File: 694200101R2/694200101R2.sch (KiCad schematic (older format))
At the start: 264 parts, among them J1 USB_C_Receptacle_USB2.0, J2 Conn_01x06_Male, J3 Conn_01x02_Male, SW1 MX_SW, SW10 MX_SW, SW100 MX_SW, SW101 MX_SW, SW102 MX_SW, SW103 MX_SW, SW104 MX_SW, SW105 MX_SW, SW106 MX_SW, SW107 MX_SW, SW108 SW_SPST, SW109 SW_SPDT, SW11 MX_SW, SW12 MX_SW, SW13 MX_SW, SW14 MX_SW, SW15 MX_SW, SW16 MX_SW, SW17 MX_SW, SW18 MX_SW, SW19 MX_SW, SW2 MX_SW, SW20 MX_SW, SW21 MX_SW, SW22 MX_SW, SW23 MX_SW, SW24 MX_SW, SW25 MX_SW, SW26 MX_SW, SW27 MX_SW, SW28 MX_SW, SW29 MX_SW, SW3 MX_SW, SW30 MX_SW, SW31 MX_SW, SW32 MX_SW, SW33 MX_SW, SW34 MX_SW, SW35 MX_SW, SW36 MX_SW, SW37 MX_SW, SW38 MX_SW, SW39 MX_SW, SW4 MX_SW, SW40 MX_SW, SW41 MX_SW, SW42 MX_SW, SW43 MX_SW, SW44 MX_SW, SW45 MX_SW, SW46 MX_SW, SW47 MX_SW, SW48 MX_SW, SW49 MX_SW, SW5 MX_SW, SW50 MX_SW, SW51 MX_SW, SW52 MX_SW, SW53 MX_SW, SW54 MX_SW, SW55 MX_SW, SW56 MX_SW, SW57 MX_SW, SW58 MX_SW, SW59 MX_SW, SW6 MX_SW, SW60 MX_SW, SW61 MX_SW, SW62 MX_SW, SW63 MX_SW, SW64 MX_SW, SW65 MX_SW, SW66 MX_SW, SW67 MX_SW, SW68 MX_SW, SW69 MX_SW, SW7 MX_SW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

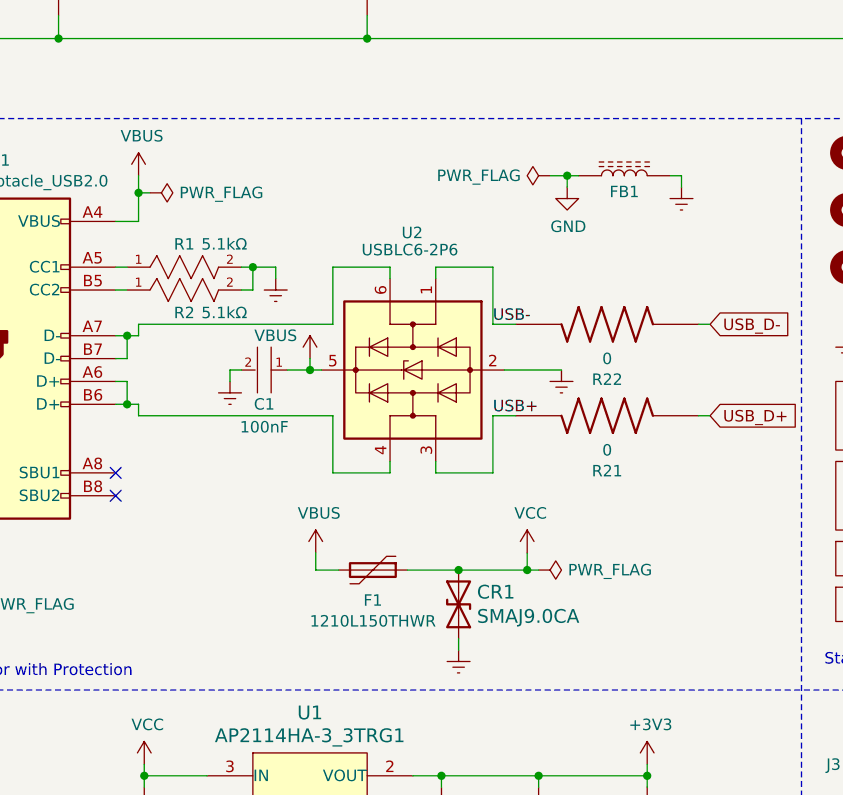
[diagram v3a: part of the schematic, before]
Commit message: Fix Ferrite Bead Placement
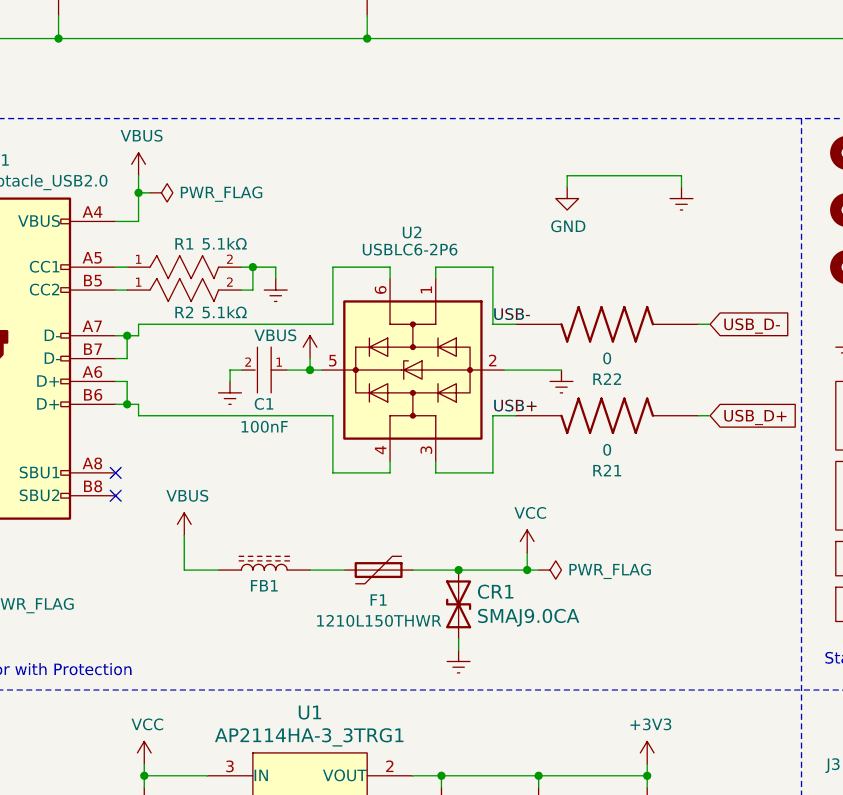
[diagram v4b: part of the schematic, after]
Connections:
- net Earth: now also C10.2, C2.2, C25.2, C3.2, C4.2, C5.2, C6.2, C7.2, C9.2, ENC1.3, ENC1.C (COM), J2.2 (Pin_2), R23.2, SW108.2 (B), U1.1 (GND), U1.4 (GND), U3.12 (VSSA), U3.18 (VSS), U3.31 (VSS), U3.47 (VSS), U3.63 (VSS), U4.1 (A0), U4.3 (A2), U4.4 (GND), U4.7 (WP), Y1.2 (GND), Y1.4 (GND); no longer FB1.1
- net VBUS: now also FB1.2; no longer F1.2
- removed net GND: C10.2, C2.2, C25.2, C3.2, C4.2, C5.2, C6.2, C7.2, C9.2, ENC1.3, ENC1.C (COM), FB1.2, J2.2 (Pin_2), R23.2, SW108.2 (B), U1.1 (GND), U1.4 (GND), U3.12 (VSSA), U3.18 (VSS), U3.31 (VSS), U3.47 (VSS), U3.63 (VSS), U4.1 (A0), U4.3 (A2), U4.4 (GND), U4.7 (WP), Y1.2 (GND), Y1.4 (GND)
- new net: F1.2, FB1.1
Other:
- moved on the sheet: F1, FB1
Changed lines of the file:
@@
 	3550 6875 3550 6800
 Wire Wire Line
-	2625 6800 2625 6875
+	2050 6725 2050 6875
 $Comp
 L power:PWR_FLAG #FLG0102
@@
 L Device:Polyfuse F1
 U 1 1 65E04245
-P 2875 6875
-F 0 "F1" V 3008 6875 50  0000 C CNN
-F 1 "1210L150THWR" V 3099 6875 50  0000 C CNN
-F 2 "Fuse:Fuse_1210_3225Metric_Castellated" H 2925 6675 50  0001 L CNN
-F 3 "~" H 2875 6875 50  0001 C CNN
-	1    2875 6875
+P 2900 6875
+F 0 "F1" V 3033 6875 50  0000 C CNN
+F 1 "1210L150THWR" V 3124 6875 50  0000 C CNN
+F 2 "Fuse:Fuse_1210_3225Metric_Castellated" H 2950 6675 50  0001 L CNN
+F 3 "~" H 2900 6875 50  0001 C CNN
+	1    2900 6875
 	0    1    1    0
 $EndComp
@@
 NoConn ~ 10775 7975
 $Comp
-L power:PWR_FLAG #FLG0104
-U 1 1 6796B8B4
-P 3650 5150
-F 0 "#FLG0104" H 3650 5225 50  0001 C CNN
-F 1 "PWR_FLAG" V 3650 5277 50  0000 L CNN
-F 2 "" H 3650 5150 50  0001 C CNN
-F 3 "~" H 3650 5150 50  0001 C CNN
-	1    3650 5150
-	0    -1   -1   0
-$EndComp
-Wire Wire Line
-	3650 5150 3725 5150
-Connection ~ 3725 5150
-$Comp
 L Power_Protection:USBLC6-2P6 U2
 U 1 1 67AF17E5
@@
 L cldg:BBUP00160808600Y00 FB1
 U 1 1 604967EC
-P 3925 5250
-F 0 "FB1" H 3875 5250 50  0000 C BNN
-F 1 "BBUP00160808600Y00" H 3875 5484 50  0001 C CNN
-F 2 "Resistor_SMD:R_0603_1608Metric" H 3925 5250 50  0001 C CNN
-F 3 "" H 3925 5250 50  0001 C CNN
-	1    3925 5250
+P 2350 6975
+F 0 "FB1" H 2300 6975 50  0000 C BNN
+F 1 "BBUP00160808600Y00" H 2300 7209 50  0001 C CNN
+F 2 "Resistor_SMD:R_0603_1608Metric" H 2350 6975 50  0001 C CNN
+F 3 "" H 2350 6975 50  0001 C CNN
+	1    2350 6975
 	-1   0    0    -1
 $EndComp
@@
 L power:VBUS #PWR0112
 U 1 1 629BAD62
-P 2625 6800
-F 0 "#PWR0112" H 2625 6650 50  0001 C CNN
-F 1 "VBUS" H 2640 6973 50  0000 C CNN
-F 2 "" H 2625 6800 50  0001 C CNN
-F 3 "" H 2625 6800 50  0001 C CNN
-	1    2625 6800
-	1    0    0    -1
-$EndComp
-Wire Wire Line
-	3725 5150 3775 5150
-Wire Wire Line
-	4175 5150 4225 5150
-Wire Wire Line
-	3025 6875 3250 6875
-Wire Wire Line
-	2625 6875 2725 6875
+P 2050 6725
+F 0 "#PWR0112" H 2050 6575 50  0001 C CNN
+F 1 "VBUS" H 2065 6898 50  0000 C CNN
+F 2 "" H 2050 6725 50  0001 C CNN
+F 3 "" H 2050 6725 50  0001 C CNN
+	1    2050 6725
+	1    0    0    -1
+$EndComp
+Wire Wire Line
+	3050 6875 3250 6875
 Wire Wire Line
 	3250 6875 3550 6875
@@
 Text Notes 11725 8925 0    50   ~ 0
 EEPROM - User Settings Storage
+Wire Wire Line
+	2600 6875 2750 6875
+Wire Wire Line
+	2050 6875 2200 6875
+Wire Wire Line
+	3725 5150 4225 5150
 $EndSCHEMATC

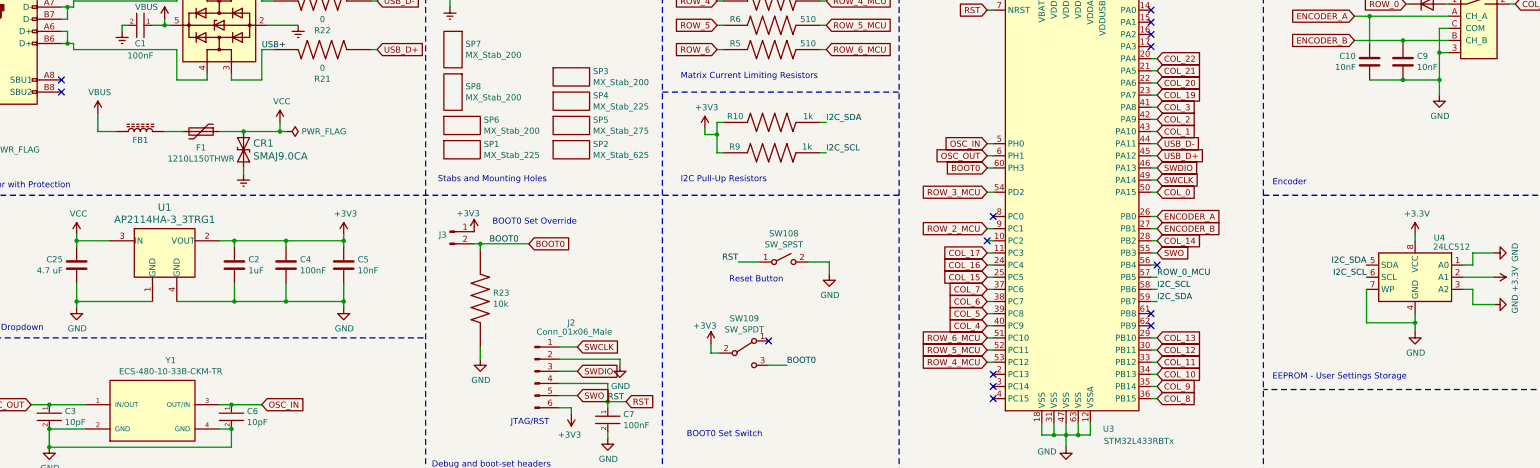
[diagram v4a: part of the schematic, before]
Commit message: Updated Address in schematic
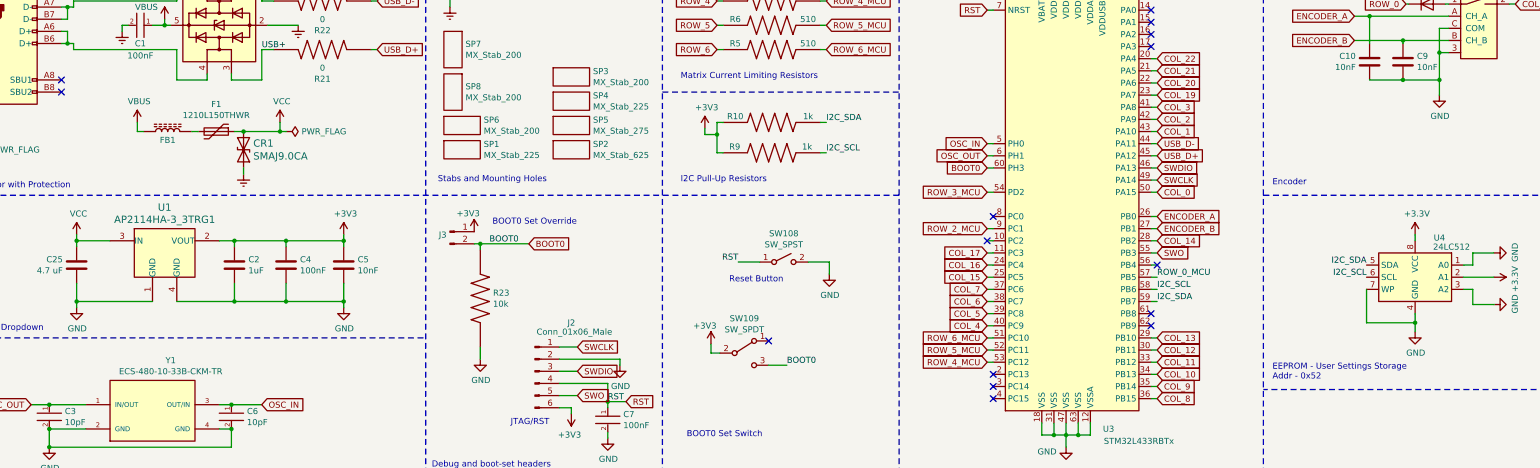
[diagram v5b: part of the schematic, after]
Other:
- note added: "EEPROM - User Settings Storage\nAddr - 0x52"
- note removed: "EEPROM - User Settings Storage"
- moved on the sheet: F1, FB1
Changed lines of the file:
@@
 	3550 6875 3550 6800
 Wire Wire Line
-	2050 6725 2050 6875
+	2375 6800 2375 6875
 $Comp
 L power:PWR_FLAG #FLG0102
@@
 L Device:Polyfuse F1
 U 1 1 65E04245
-P 2900 6875
-F 0 "F1" V 3033 6875 50  0000 C CNN
-F 1 "1210L150THWR" V 3124 6875 50  0000 C CNN
-F 2 "Fuse:Fuse_1210_3225Metric_Castellated" H 2950 6675 50  0001 L CNN
-F 3 "~" H 2900 6875 50  0001 C CNN
-	1    2900 6875
+P 3025 6875
+F 0 "F1" V 2800 6875 50  0000 C CNN
+F 1 "1210L150THWR" V 2891 6875 50  0000 C CNN
+F 2 "Fuse:Fuse_1210_3225Metric_Castellated" H 3075 6675 50  0001 L CNN
+F 3 "~" H 3025 6875 50  0001 C CNN
+	1    3025 6875
 	0    1    1    0
 $EndComp
@@
 L cldg:BBUP00160808600Y00 FB1
 U 1 1 604967EC
-P 2350 6975
-F 0 "FB1" H 2300 6975 50  0000 C BNN
-F 1 "BBUP00160808600Y00" H 2300 7209 50  0001 C CNN
-F 2 "Resistor_SMD:R_0603_1608Metric" H 2350 6975 50  0001 C CNN
-F 3 "" H 2350 6975 50  0001 C CNN
-	1    2350 6975
+P 2575 6975
+F 0 "FB1" H 2525 6975 50  0000 C BNN
+F 1 "BBUP00160808600Y00" H 2525 7209 50  0001 C CNN
+F 2 "Resistor_SMD:R_0603_1608Metric" H 2575 6975 50  0001 C CNN
+F 3 "" H 2575 6975 50  0001 C CNN
+	1    2575 6975
 	-1   0    0    -1
 $EndComp
@@
 L power:VBUS #PWR0112
 U 1 1 629BAD62
-P 2050 6725
-F 0 "#PWR0112" H 2050 6575 50  0001 C CNN
-F 1 "VBUS" H 2065 6898 50  0000 C CNN
-F 2 "" H 2050 6725 50  0001 C CNN
-F 3 "" H 2050 6725 50  0001 C CNN
-	1    2050 6725
-	1    0    0    -1
-$EndComp
-Wire Wire Line
-	3050 6875 3250 6875
+P 2375 6800
+F 0 "#PWR0112" H 2375 6650 50  0001 C CNN
+F 1 "VBUS" H 2390 6973 50  0000 C CNN
+F 2 "" H 2375 6800 50  0001 C CNN
+F 3 "" H 2375 6800 50  0001 C CNN
+	1    2375 6800
+	1    0    0    -1
+$EndComp
+Wire Wire Line
+	3175 6875 3250 6875
 Wire Wire Line
 	3250 6875 3550 6875
@@
 	14375 4900 14375 9000
 Text Notes 11725 8925 0    50   ~ 0
-EEPROM - User Settings Storage
-Wire Wire Line
-	2600 6875 2750 6875
-Wire Wire Line
-	2050 6875 2200 6875
+EEPROM - User Settings Storage\nAddr - 0x52
+Wire Wire Line
+	2825 6875 2875 6875
+Wire Wire Line
+	2375 6875 2425 6875
 Wire Wire Line
 	3725 5150 4225 5150

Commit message: sch review
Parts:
- removed J3: Conn_01x02_Male, Connector_PinHeader_2.54mm:PinHeader_1x02_P2.54mm_Vertical, symbol Connector:Conn_01x02_Male
- C2: value 1uF -> 4.7 uF; footprint Capacitor_SMD:C_0603_1608Metric -> Capacitor_SMD:C_0805_2012Metric
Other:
- note removed: "BOOT0 Set Override"
- moved on the sheet: C7, J2, R23, SW108, SW109
